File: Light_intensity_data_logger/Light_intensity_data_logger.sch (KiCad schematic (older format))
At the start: 23 parts, among them J1 Wire_to_Vbat, Q1 NTJD4001NT1G, Q2 NTJD4001NT1G, U1 BME280, U2 TSL25911FN, U3 TCS34725FN, U4 Teensy3.6

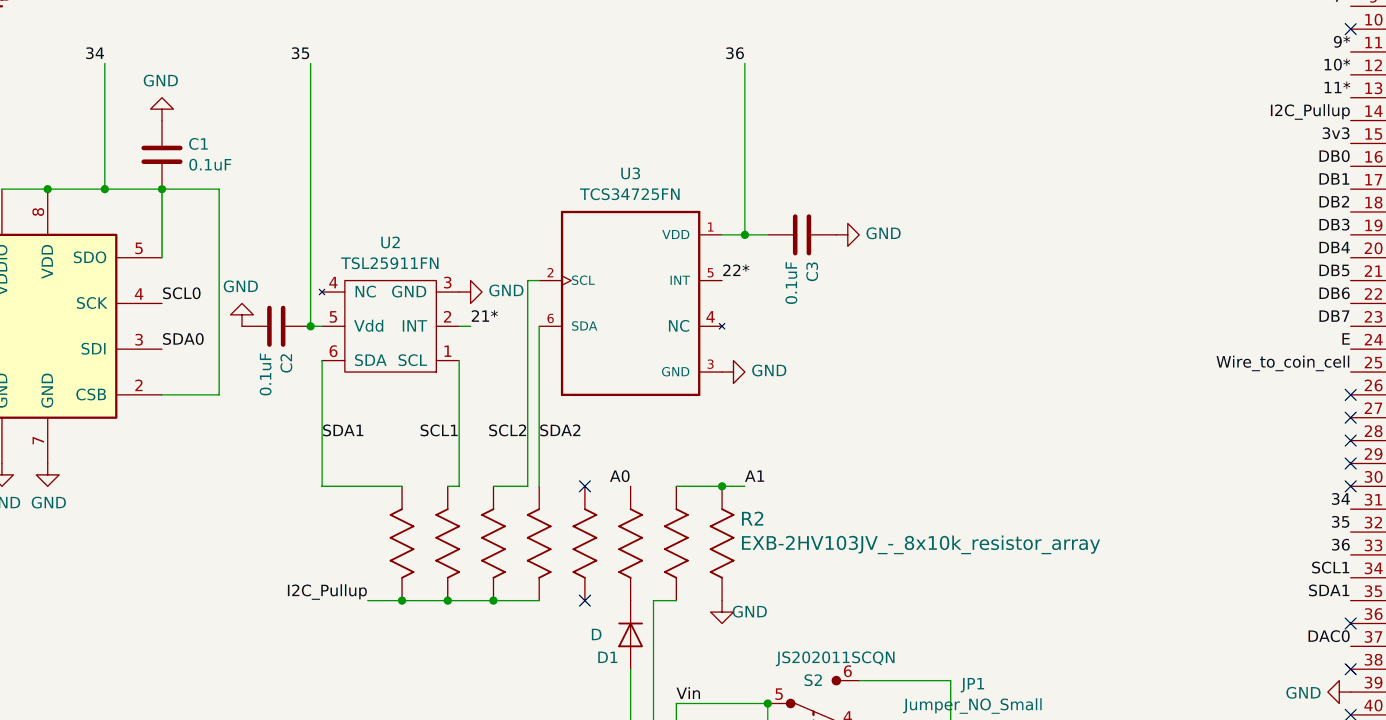
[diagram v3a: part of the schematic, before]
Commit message: Teensy flipped sensors rewired
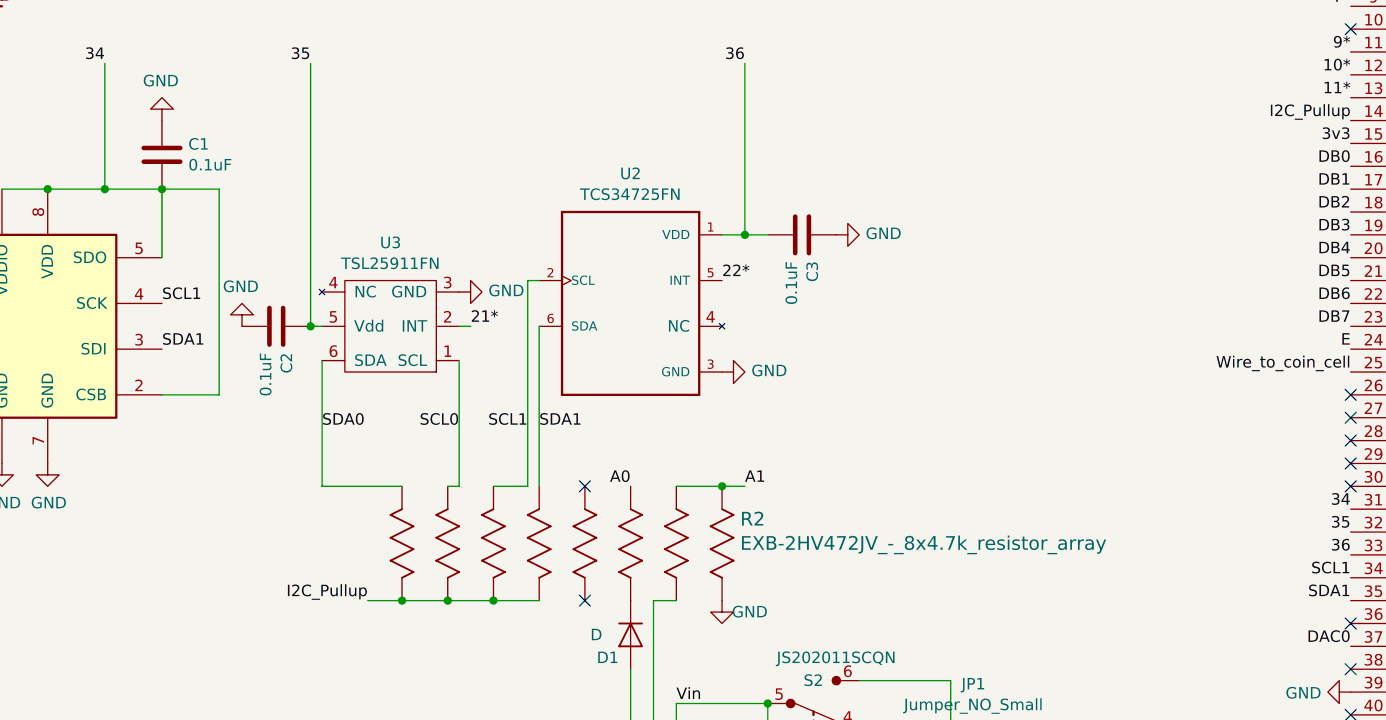
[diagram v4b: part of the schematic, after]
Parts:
- R2: value EXB-2HV103JV_-_8x10k_resistor_array -> EXB-2HV472JV_-_8x4.7k_resistor_array; Part# Y1103CT-ND -> Y1472CT-ND
- renumbered U3 to U2, U2 to U3
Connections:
- net SCL0: now also R2.7, U3.1 (SCL); no longer U1.4 (SCK)
- net SCL1: now also R2.6, U1.4 (SCK), U2.2 (SCL); no longer R2.7, U3.1 (SCL)
- net SCL2: no longer R2.6, U2.2 (SCL)
- net SDA0: now also R2.8, U3.6 (SDA); no longer U1.3 (SDI)
- net SDA1: now also R2.5, U1.3 (SDI), U2.6 (SDA); no longer R2.8, U3.6 (SDA)
- net SDA2: no longer R2.5, U2.6 (SDA)
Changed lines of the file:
@@
 Text Label 10950 4350 0    50   ~ 0
 Vin
-$Comp
-L power:GND #PWR0101
-U 1 1 5E1EC75C
-P 5500 5950
-F 0 "#PWR0101" H 5500 5700 50  0001 C CNN
-F 1 "GND" H 5505 5777 50  0000 C CNN
-F 2 "" H 5500 5950 50  0001 C CNN
-F 3 "" H 5500 5950 50  0001 C CNN
-	1    5500 5950
-	1    0    0    -1
-$EndComp
-$Comp
-L Ben_custom:BU2032SM-BT-GTR BT1
-U 1 1 5E1F3175
-P 5500 5650
-F 0 "BT1" H 5454 5780 50  0000 L CNN
-F 1 "BU2032SM-BT-GTR" H 5250 5850 50  0000 L CNN
-F 2 "Ben_Custom:BU2032SM-BT-GTR" H 5150 5200 50  0001 L BNN
-F 3 "http://www.memoryprotectiondevices.com/datasheets/BU2032SM-BT-GTR-datasheet.pdf" H 4900 5300 50  0001 L BNN
-F 4 "BU2032SM-BT-GCT-ND" H 5100 5100 50  0001 L BNN "Part#"
-	1    5500 5650
-	0    1    1    0
-$EndComp
 Text Label 10950 4550 0    50   ~ 0
 3v3
@@
 	1    0    0    -1
 $EndComp
-Text Label 3450 3150 0    50   ~ 0
-SDA0
 Text Label 10950 5050 0    50   ~ 0
-SCL0
-Text Label 3450 2950 0    50   ~ 0
 SCL0
 Text Label 8650 4250 2    50   ~ 0
@@
 	1    2650 1350
 	0    1    1    0
-$EndComp
-$Comp
-L device:D D1
-U 1 1 5E2E8394
-P 5500 4400
-F 0 "D1" V 5600 4500 50  0000 C CNN
-F 1 "D" V 5500 4550 50  0000 C CNN
-F 2 "Diodes_SMD:D_SOD-323" H 5500 4400 50  0001 C CNN
-F 3 "https://toshiba.semicon-storage.com/info/docget.jsp?did=14077&prodName=CUS10S30" H 5500 4400 50  0001 C CNN
-F 4 "CUS10S30H3FCT-ND" H 5500 4400 50  0001 C CNN "Part#"
-	1    5500 4400
-	0    -1   1    0
 $EndComp
 Wire Wire Line
@@
 Current test
 Wire Wire Line
-	5500 4550 5500 4950
-Wire Wire Line
 	5700 5350 5600 5350
 Wire Wire Line
@@
 P 5900 3750
 F 0 "R2" V 6044 3829 60  0000 L CNN
-F 1 "EXB-2HV103JV_-_8x10k_resistor_array" V 6150 3829 60  0000 L CNN
+F 1 "EXB-2HV472JV_-_8x4.7k_resistor_array" V 6150 3829 60  0000 L CNN
 F 2 "Ben_Custom:Resistor_array_1506_8x" H 6150 3415 60  0001 C CNN
-F 3 "https://industrial.panasonic.com/cdbs/www-data/pdf/AOC0000/AOC0000C14.pdf" V 6650 4200 60  0001 L CNN
-F 4 "Y1103CT-ND" V 5900 3750 50  0001 C CNN "Part#"
+F 3 "https://industrial.panasonic.com/cdbs/www-https://industrial.panasonic.com/cdbs/www-data/pdf/AOC0000/AOC0000C14.pdf" V 6650 4200 60  0001 L CNN
+F 4 "Y1472CT-ND" V 5900 3750 50  0001 C CNN "Part#"
 	1    5900 3750
 	0    1    1    0
@@
 Wire Wire Line
 	5100 3050 5100 3750
-Text Label 5050 3550 2    50   ~ 0
-SCL2
-Text Label 5100 3550 0    50   ~ 0
-SDA2
 Text Label 8650 1250 2    50   ~ 0
 SCL2
@@
 Text Label 8650 1550 2    50   ~ 0
 6*
-Text Label 4150 3550 0    50   ~ 0
+Text Label 3450 3150 0    50   ~ 0
 SDA1
-Text Label 4750 3550 2    50   ~ 0
+Text Label 5050 3500 2    50   ~ 0
 SCL1
 Text Label 8650 4150 2    50   ~ 0
@@
 3v3
 $Comp
-L Ben_custom:TSL25911FN U2
+L Ben_custom:TSL25911FN U3
 U 1 1 5E1E6521
 P 4450 3050
-F 0 "U2" H 4450 2685 50  0000 C CNN
+F 0 "U3" H 4450 2685 50  0000 C CNN
 F 1 "TSL25911FN" H 4450 2776 50  0000 C CNN
 F 2 "Ben_Custom:TSL25911FN" H 4050 3500 50  0001 C CNN
@@
 $EndComp
 $Comp
-L Ben_custom:TCS34725FN U3
+L Ben_custom:TCS34725FN U2
 U 1 1 5E1E525D
 P 5500 2950
-F 0 "U3" H 5500 3517 50  0000 C CNN
+F 0 "U2" H 5500 3517 50  0000 C CNN
 F 1 "TCS34725FN" H 5500 3426 50  0000 C CNN
 F 2 "Ben_Custom:TCS34725" H 5150 3450 50  0001 L BNN
@@
 Text Label 10950 5150 0    50   ~ 0
 SDA0
+Text Label 4750 3500 2    50   ~ 0
+SCL0
+Text Label 4150 3500 0    50   ~ 0
+SDA0
+Wire Wire Line
+	5500 4550 5500 4950
+$Comp
+L power:GND #PWR0101
+U 1 1 5E1EC75C
+P 5500 5950
+F 0 "#PWR0101" H 5500 5700 50  0001 C CNN
+F 1 "GND" H 5505 5777 50  0000 C CNN
+F 2 "" H 5500 5950 50  0001 C CNN
+F 3 "" H 5500 5950 50  0001 C CNN
+	1    5500 5950
+	1    0    0    -1
+$EndComp
+$Comp
+L Ben_custom:BU2032SM-BT-GTR BT1
+U 1 1 5E1F3175
+P 5500 5650
+F 0 "BT1" H 5454 5780 50  0000 L CNN
+F 1 "BU2032SM-BT-GTR" H 5250 5850 50  0000 L CNN
+F 2 "Ben_Custom:BU2032SM-BT-GTR" H 5150 5200 50  0001 L BNN
+F 3 "http://www.memoryprotectiondevices.com/datasheets/BU2032SM-BT-GTR-datasheet.pdf" H 4900 5300 50  0001 L BNN
+F 4 "BU2032SM-BT-GCT-ND" H 5100 5100 50  0001 L BNN "Part#"
+	1    5500 5650
+	0    1    1    0
+$EndComp
+$Comp
+L device:D D1
+U 1 1 5E2E8394
+P 5500 4400
+F 0 "D1" V 5600 4500 50  0000 C CNN
+F 1 "D" V 5500 4550 50  0000 C CNN
+F 2 "Diodes_SMD:D_SOD-323" H 5500 4400 50  0001 C CNN
+F 3 "https://toshiba.semicon-storage.com/info/docget.jsp?did=14077&prodName=CUS10S30" H 5500 4400 50  0001 C CNN
+F 4 "CUS10S30H3FCT-ND" H 5500 4400 50  0001 C CNN "Part#"
+	1    5500 4400
+	0    -1   1    0
+$EndComp
+Text Label 3450 2950 0    50   ~ 0
+SCL1
+Text Label 5100 3500 0    50   ~ 0
+SDA1
 $EndSCHEMATC

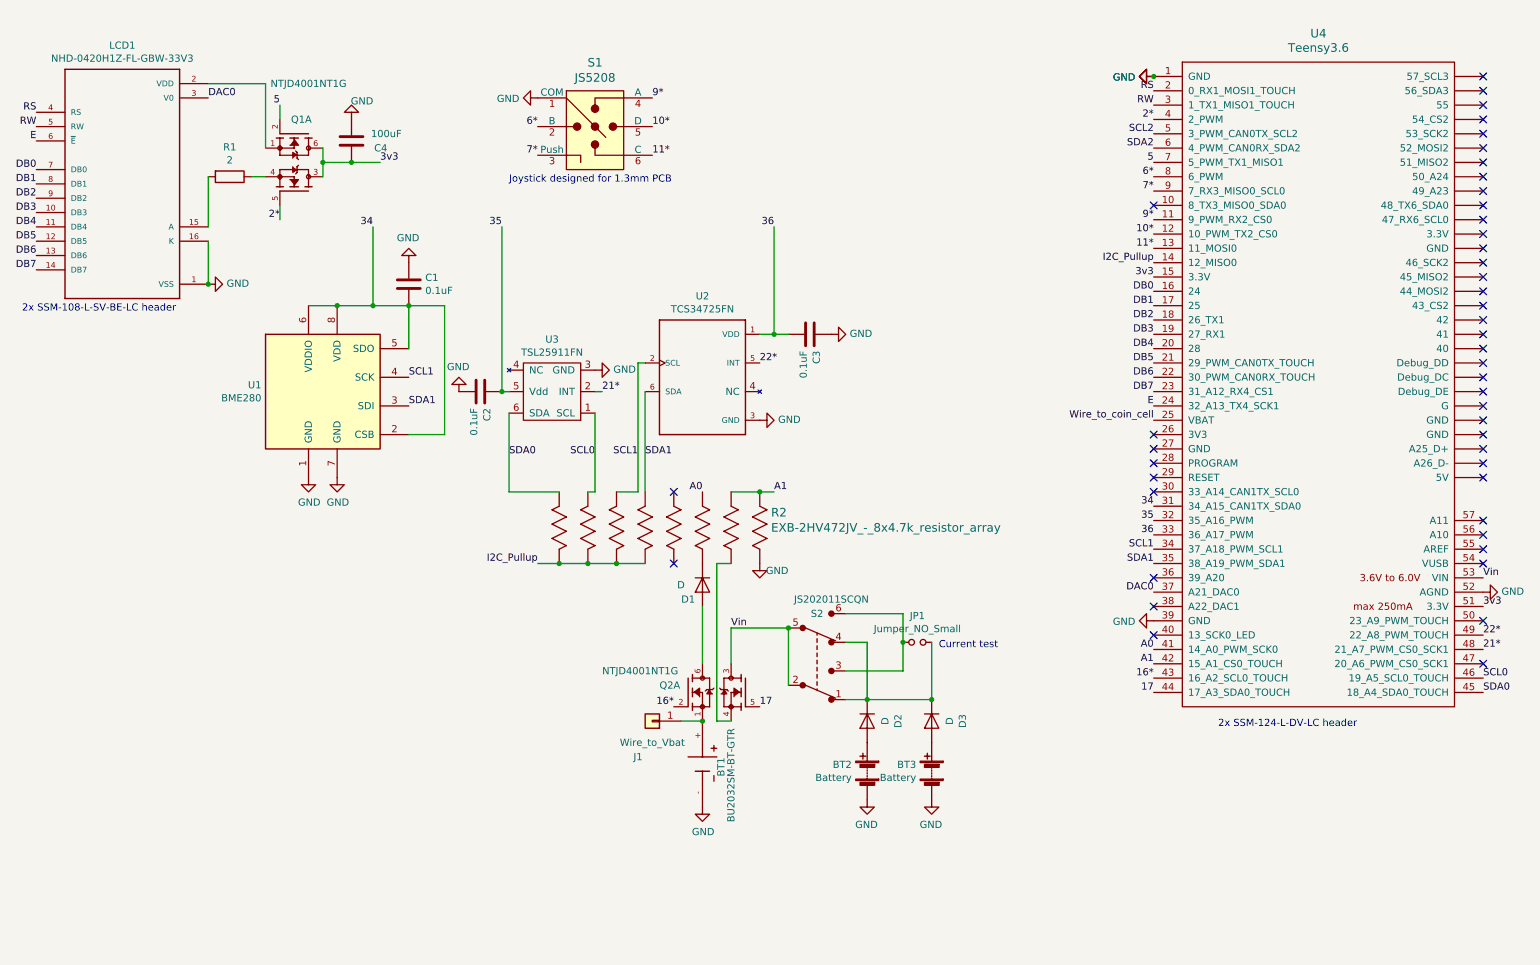
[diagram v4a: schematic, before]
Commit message: All but left monitor wired
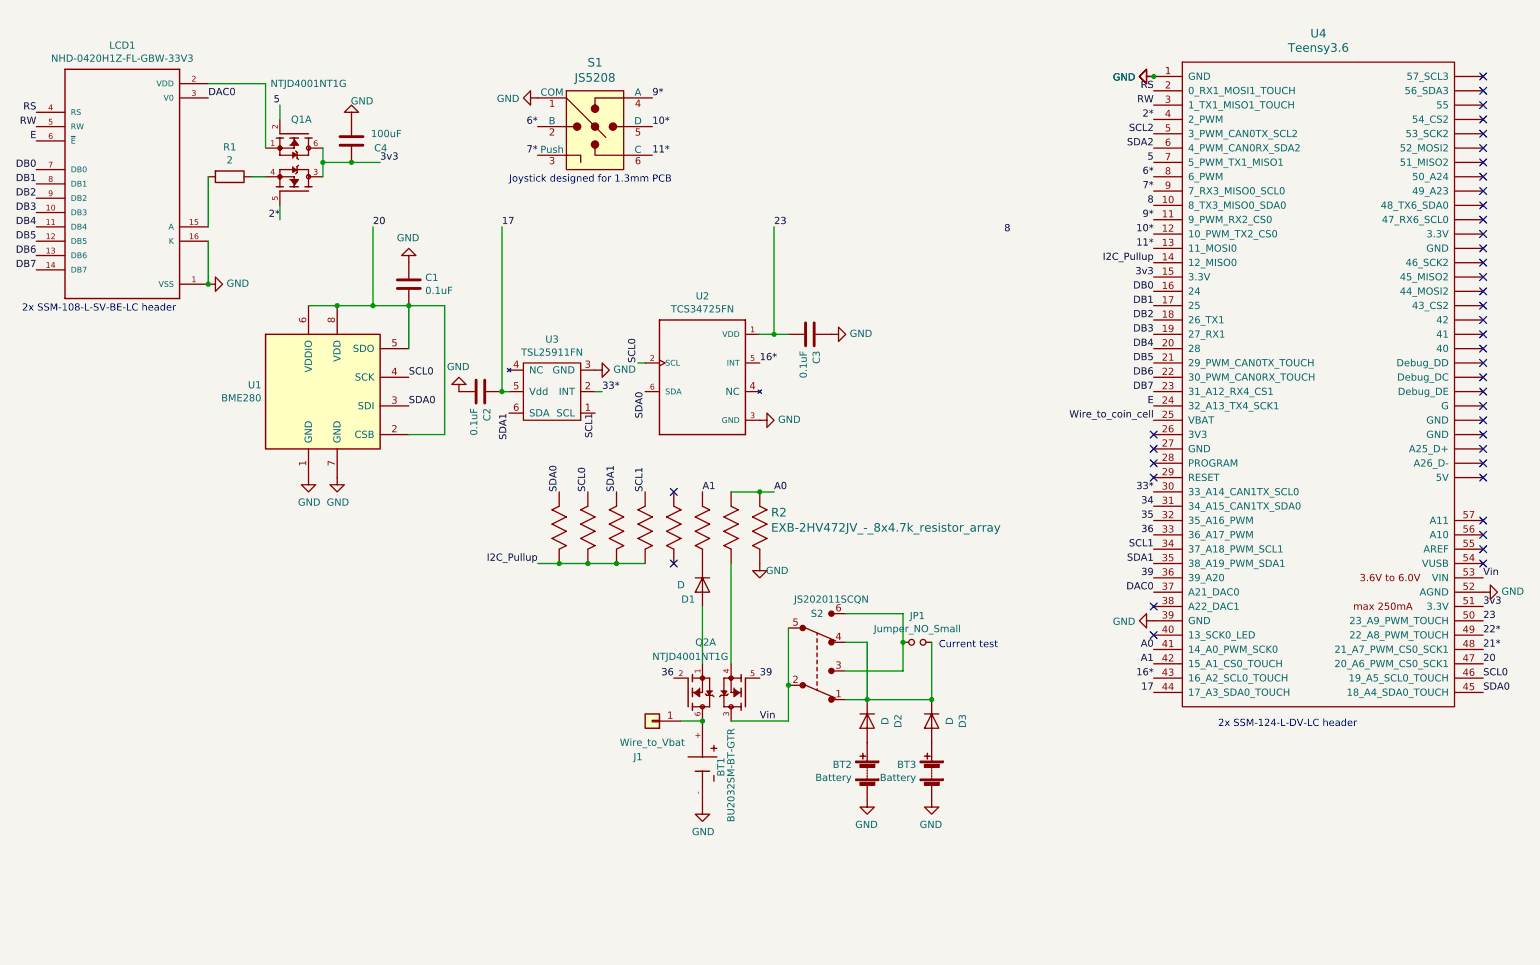
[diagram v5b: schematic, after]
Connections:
- net 16*: now also U2.5 (INT); no longer Q2.2 (G1)
- net 17: now also C2.1, U3.5 (Vdd); no longer Q2.5 (G2)
- net 21*: no longer U3.2 (INT)
- net 22*: no longer U2.5 (INT)
- net 34: no longer C1.2, U1.2 (CSB), U1.5 (SDO), U1.6 (VDDIO), U1.8 (VDD)
- net 35: no longer C2.1, U3.5 (Vdd)
- net 36: now also Q2.2 (G1); no longer C3.2, U2.1 (VDD)
- net A0: now also R2.1, R2.2; no longer R2.3
- net A1: now also R2.3; no longer R2.1, R2.2
- net SCL0: now also U1.4 (SCK), U2.2 (SCL); no longer U3.1 (SCL)
- net SCL1: now also R2.5, U3.1 (SCL); no longer R2.6, U1.4 (SCK), U2.2 (SCL)
- net SDA0: now also U1.3 (SDI), U2.6 (SDA); no longer U3.6 (SDA)
- net SDA1: now also R2.6, U3.6 (SDA); no longer R2.5, U1.3 (SDI), U2.6 (SDA)
- net at BT1.+, J1.1 (Pin_1): now also Q2.6 (D1); no longer Q2.1 (S1)
- net at D1.2 (A): now also Q2.1 (S1); no longer Q2.6 (D1)
- net 8: now reaches U4.10 (8_TX3_MISO0_SDA0)
- net 33*: now reaches U4.30 (33_A14_CAN1TX_SCL0)
- net 33*: now also U3.2 (INT)
- net 39: now reaches U4.36 (39_A20)
- net 39: now also Q2.5 (G2)
- net 20: now reaches U4.47 (20_A6_PWM_CS0_SCK1)
- net 20: now also C1.2, U1.2 (CSB), U1.5 (SDO), U1.6 (VDDIO), U1.8 (VDD)
- net 23: now reaches U4.50 (23_A9_PWM_TOUCH)
- net 23: now also C3.2, U2.1 (VDD)
- no-connect marks 46 -> 41
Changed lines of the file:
@@
 Text Label 8650 4250 2    50   ~ 0
 SDA1
-NoConn ~ 8650 4350
 NoConn ~ 8650 4550
 NoConn ~ 8650 4750
@@
 	5350 5350 5500 5350
 $Comp
-L Ben_custom:NTJD4001NT1G Q2
-U 1 1 5E2C265D
-P 5500 5150
-F 0 "Q2" H 5200 5200 50  0000 L CNN
-F 1 "NTJD4001NT1G" H 4800 5300 50  0000 L CNN
-F 2 "TO_SOT_Packages_SMD:SOT-363_SC-70-6" H 4750 5000 50  0001 L BNN
-F 3 "http://www.onsemi.com/pub/Collateral/NTJD4001N-D.PDF" H 5400 5150 50  0001 L BNN
-F 4 "NTJD4001NT1GOSCT-ND" H 5400 5150 50  0001 L BNN "Part#"
-	1    5500 5150
-	1    0    0    -1
-$EndComp
-$Comp
 L dk_Slide-Switches:JS202011SCQN S2
 U 1 1 5E261D45
@@
 	-1   0    0    -1
 $EndComp
-Text Label 5700 4700 0    50   ~ 0
+Text Label 5900 5350 0    50   ~ 0
 Vin
 $Comp
@@
 Text Notes 7150 4850 0    50   ~ 0
 Current test
-Wire Wire Line
-	5700 5350 5600 5350
-Wire Wire Line
-	5600 5350 5600 4250
-Wire Wire Line
-	5600 4250 5700 4250
-Connection ~ 5500 5350
-Text Label 3200 1900 2    50   ~ 0
-34
 Text Label 8650 4850 2    50   ~ 0
 A0
@@
 Text Label 8650 5150 2    50   ~ 0
 17
-Text Label 5300 5250 2    50   ~ 0
+Text Label 5900 2850 0    50   ~ 0
 16*
-Text Label 5900 5250 0    50   ~ 0
+Text Label 4100 1900 0    50   ~ 0
 17
 $Comp
@@
 Text Label 2550 1050 2    50   ~ 0
 5
-NoConn ~ 10950 4650
-NoConn ~ 10950 4950
 $Comp
 L conn:Conn_01x01 J1
@@
 	-1   0    0    1
 $EndComp
-Wire Wire Line
-	6100 5100 6100 4700
-Connection ~ 6100 4700
-Wire Wire Line
-	5700 4700 5700 4950
 Wire Wire Line
 	4700 4250 4900 4250
@@
 Text Label 8650 1450 2    50   ~ 0
 5
-Text Label 5500 3750 2    50   ~ 0
+Text Label 6000 3750 0    50   ~ 0
 A0
-Text Label 6000 3750 0    50   ~ 0
+Text Label 5500 3750 0    50   ~ 0
 A1
-Text Label 6000 1900 2    50   ~ 0
-36
-Text Label 4100 1900 2    50   ~ 0
-35
 Text Label 8650 4050 2    50   ~ 0
 36
@@
 Wire Wire Line
 	6000 3750 5900 3750
-Wire Wire Line
-	5050 3750 4900 3750
 Wire Wire Line
 	5900 2650 6000 2650
@@
 Text Label 8650 2150 2    50   ~ 0
 I2C_Pullup
-Text Label 4800 3050 0    50   ~ 0
-21*
-Text Label 5900 2850 0    50   ~ 0
-22*
 Text Label 8650 3150 2    50   ~ 0
 E
@@
 Wire Wire Line
 	4150 3050 4100 3050
-Wire Wire Line
-	4150 3750 4500 3750
-Wire Wire Line
-	4150 3200 4150 3750
-Wire Wire Line
-	4750 3200 4750 3750
-Wire Wire Line
-	4750 3750 4700 3750
 $Comp
 L power:GND #PWR0113
@@
 NoConn ~ 10950 950
 NoConn ~ 10950 850
-NoConn ~ 8650 3750
 NoConn ~ 8650 3650
 NoConn ~ 8650 3550
-NoConn ~ 8650 1750
-Wire Wire Line
-	5100 3050 5100 3750
 Text Label 8650 1250 2    50   ~ 0
 SCL2
@@
 6*
 Text Label 3450 3150 0    50   ~ 0
-SDA1
-Text Label 5050 3500 2    50   ~ 0
-SCL1
+SDA0
+Text Label 5050 2850 1    50   ~ 0
+SCL0
 Text Label 8650 4150 2    50   ~ 0
 SCL1
@@
 Wire Wire Line
 	4750 3050 4800 3050
-Wire Wire Line
-	5050 2850 5050 3750
 Wire Wire Line
 	5100 2850 5050 2850
@@
 $EndComp
 Connection ~ 7100 5200
-Wire Wire Line
-	5700 4700 6100 4700
 Text Label 10950 5150 0    50   ~ 0
 SDA0
-Text Label 4750 3500 2    50   ~ 0
-SCL0
-Text Label 4150 3500 0    50   ~ 0
-SDA0
+Text Label 4750 3200 3    50   ~ 0
+SCL1
+Text Label 4150 3200 3    50   ~ 0
+SDA1
 Wire Wire Line
 	5500 4550 5500 4950
@@
 $EndComp
 Text Label 3450 2950 0    50   ~ 0
+SCL0
+Text Label 5100 3050 3    50   ~ 0
+SDA0
+Text Label 10950 4950 0    50   ~ 0
+20
+Text Label 3200 1900 0    50   ~ 0
+20
+Text Label 10950 4650 0    50   ~ 0
+23
+Text Label 6000 1900 0    50   ~ 0
+23
+Text Label 8650 3750 2    50   ~ 0
+33*
+Text Label 4800 3050 0    50   ~ 0
+33*
+Text Label 4500 3750 1    50   ~ 0
+SDA0
+Text Label 4700 3750 1    50   ~ 0
+SCL0
+Text Label 4900 3750 1    50   ~ 0
+SDA1
+Text Label 5100 3750 1    50   ~ 0
 SCL1
-Text Label 5100 3500 0    50   ~ 0
-SDA1
+Text Label 8650 1750 2    50   ~ 0
+8
+Text Label 7650 1950 2    50   ~ 0
+8
+Text Label 5300 5050 2    50   ~ 0
+36
+Text Label 8650 4350 2    50   ~ 0
+39
+Text Label 5900 5050 0    50   ~ 0
+39
+Wire Wire Line
+	6100 5100 6100 5350
+Connection ~ 6100 5100
+Wire Wire Line
+	5700 4950 5700 4250
+$Comp
+L Ben_custom:NTJD4001NT1G Q2
+U 1 1 5E2C265D
+P 5500 5150
+F 0 "Q2" H 5450 4800 50  0000 L CNN
+F 1 "NTJD4001NT1G" H 5150 4900 50  0000 L CNN
+F 2 "TO_SOT_Packages_SMD:SOT-363_SC-70-6" H 4750 5000 50  0001 L BNN
+F 3 "http://www.onsemi.com/pub/Collateral/NTJD4001N-D.PDF" H 5400 5150 50  0001 L BNN
+F 4 "NTJD4001NT1GOSCT-ND" H 5400 5150 50  0001 L BNN "Part#"
+	1    5500 5150
+	1    0    0    1
+$EndComp
+Connection ~ 5500 5350
+Wire Wire Line
+	6100 4700 6100 5100
+Wire Wire Line
+	5700 5350 6100 5350
 $EndSCHEMATC
